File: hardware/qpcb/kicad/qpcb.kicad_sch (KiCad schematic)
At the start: 3 parts, among them J1 Conn_02x05_Odd_Even, J2 Conn_01x04, U1 Pico

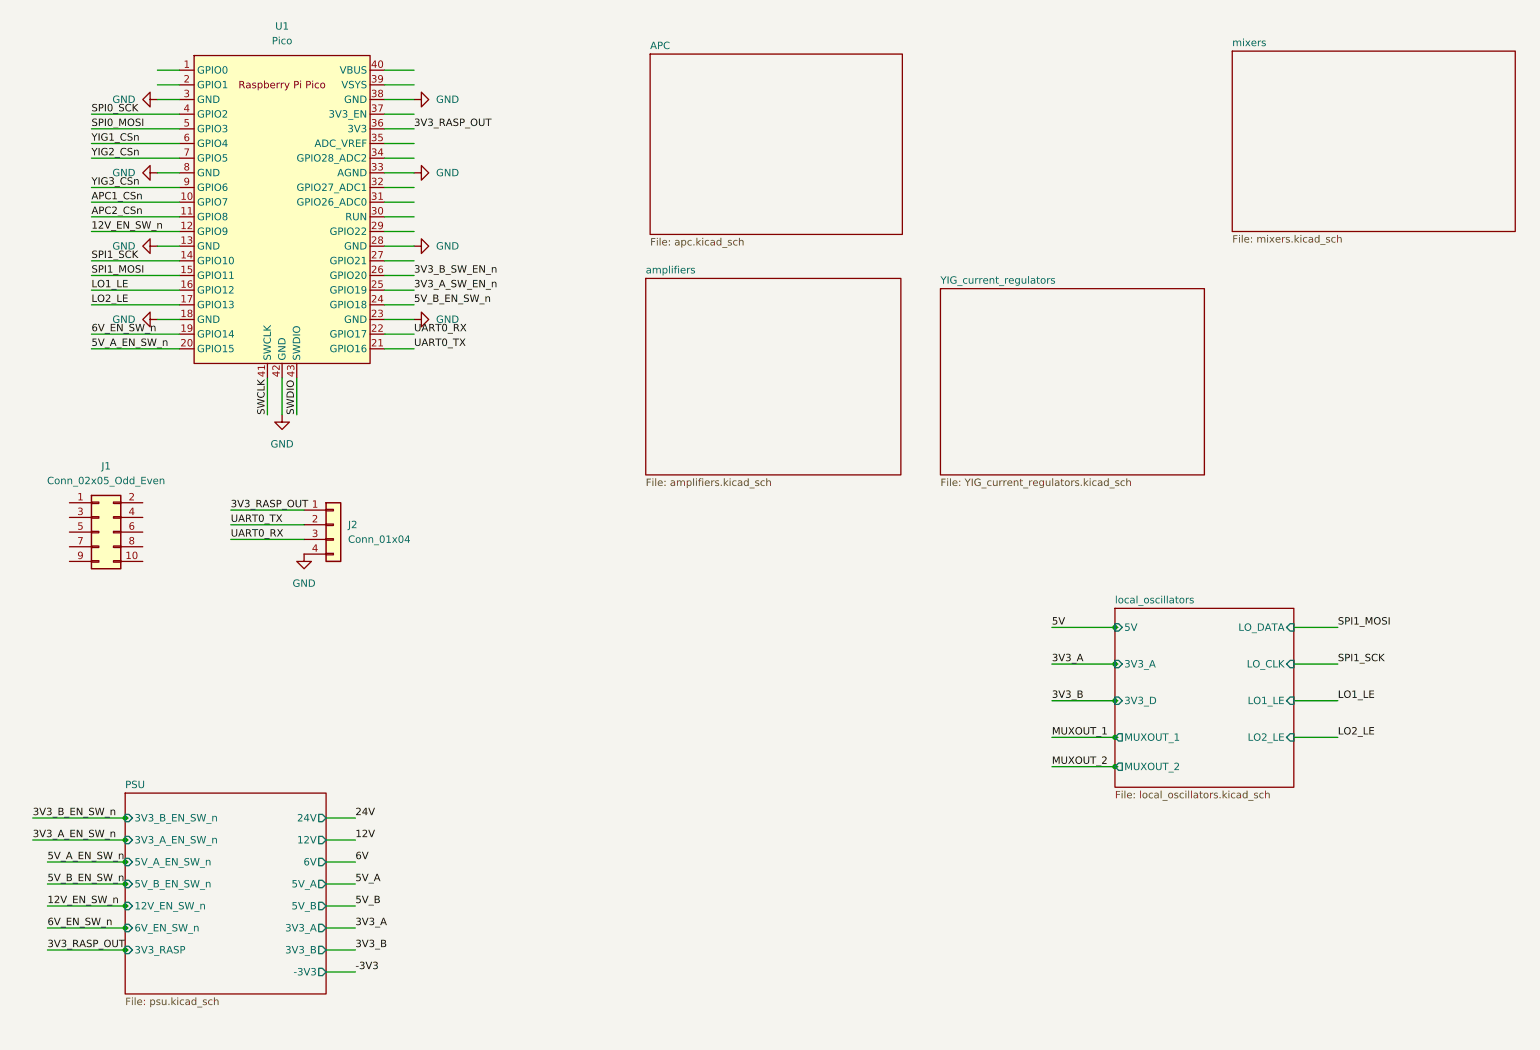
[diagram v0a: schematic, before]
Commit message: Complete PSU simulations and fix ERC errors
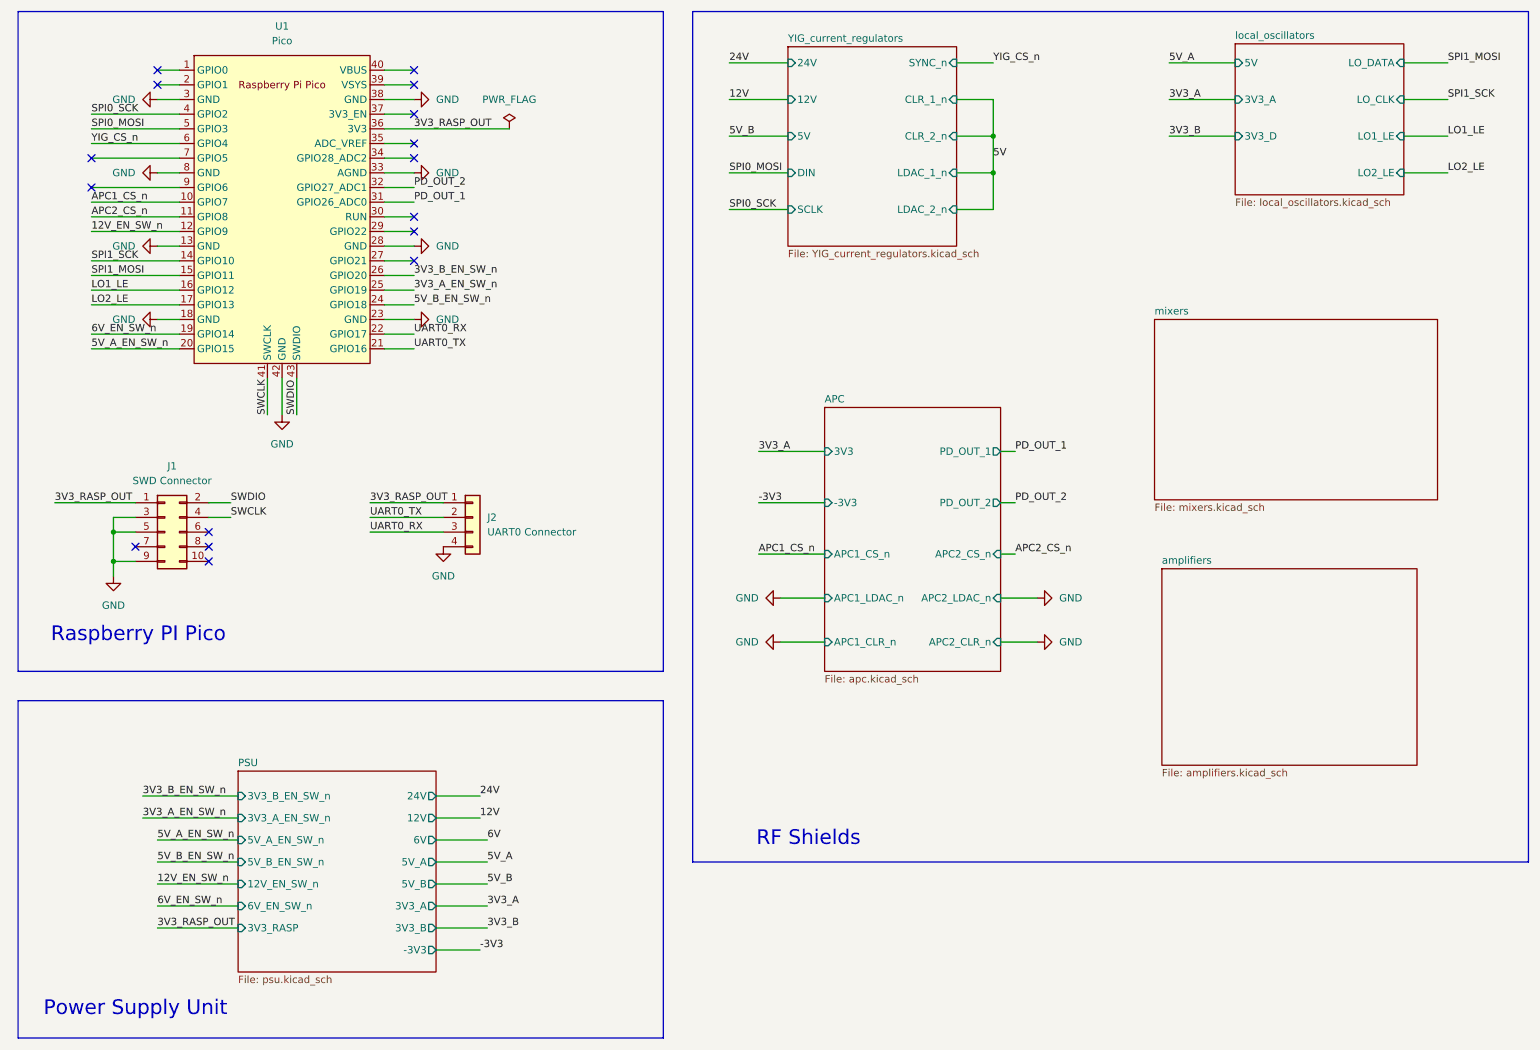
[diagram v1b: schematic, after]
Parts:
- J1: value Conn_02x05_Odd_Even -> SWD Connector
- J2: value Conn_01x04 -> UART0 Connector
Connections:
- net 3V3_A_SW_EN_n is gone; now on net 3V3_A_EN_SW_n: U1.25 (GPIO19)
- net 3V3_B_SW_EN_n is gone; now on net 3V3_B_EN_SW_n: U1.26 (GPIO20)
- net 3V3_RASP_OUT: now also J1.1 (Pin_1)
- net GND: now also J1.3 (Pin_3), J1.5 (Pin_5), J1.9 (Pin_9)
- net SWCLK: now also J1.4 (Pin_4)
- net SWDIO: now also J1.2 (Pin_2)
- net PD_OUT_1: now reaches U1.31 (GPIO26_ADC0)
- net PD_OUT_2: now reaches U1.32 (GPIO27_ADC1)
- net APC1_CSn renamed APC1_CS_n
- net APC2_CSn renamed APC2_CS_n
- net YIG1_CSn renamed YIG_CS_n
- net YIG2_CSn: no longer names the net of U1.7 (GPIO5)
- net YIG3_CSn: no longer names the net of U1.9 (GPIO6)
- no-connect marks 0 -> 16
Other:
- sheet APC ports: added -3V3, 3V3, APC1_CLR_n, APC1_CS_n, APC1_LDAC_n, APC2_CLR_n, APC2_CS_n, APC2_LDAC_n, PD_OUT_1, PD_OUT_2; removed none
- sheet YIG_current_regulators ports: added 12V, 24V, 5V, CLR_1_n, CLR_2_n, DIN, LDAC_1_n, LDAC_2_n, SCLK, SYNC_n; removed none
- sheet local_oscillators ports: added none; removed MUXOUT_1, MUXOUT_2
- note added: "Power Supply Unit"
- note added: "RF Shields"
- note added: "Raspberry PI Pico"
- moved on the sheet: J1, J2

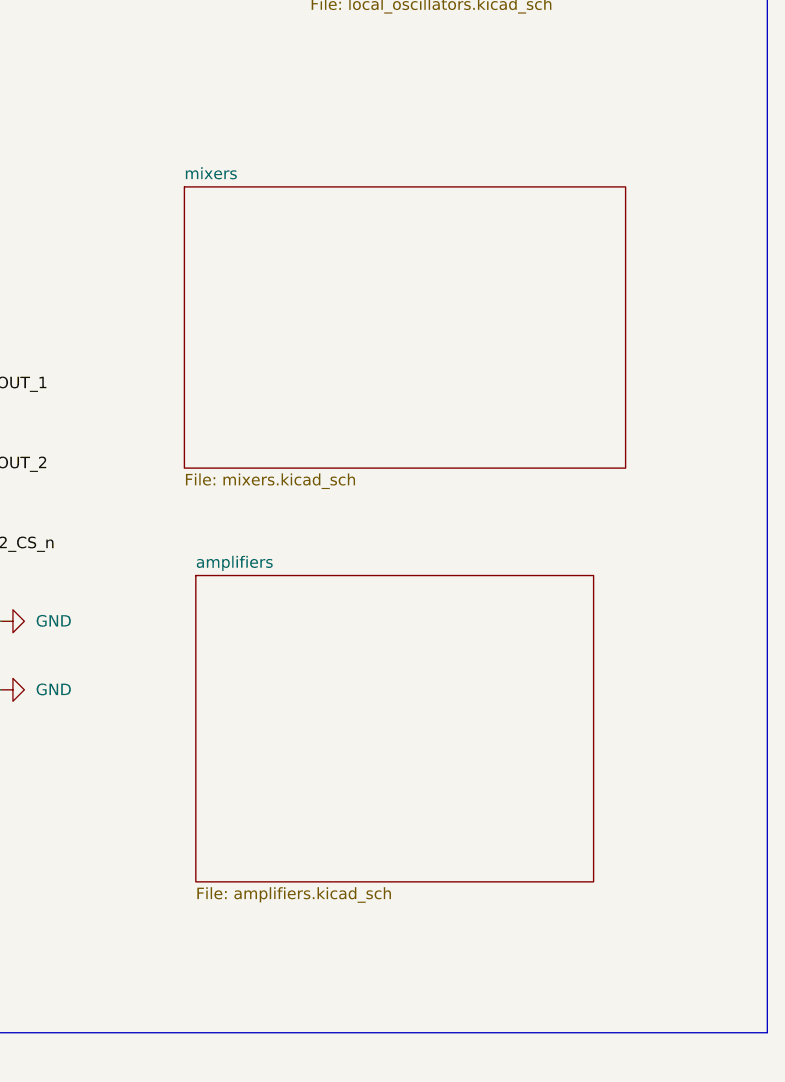
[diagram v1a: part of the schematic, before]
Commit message: Add mixer footprint and symbols
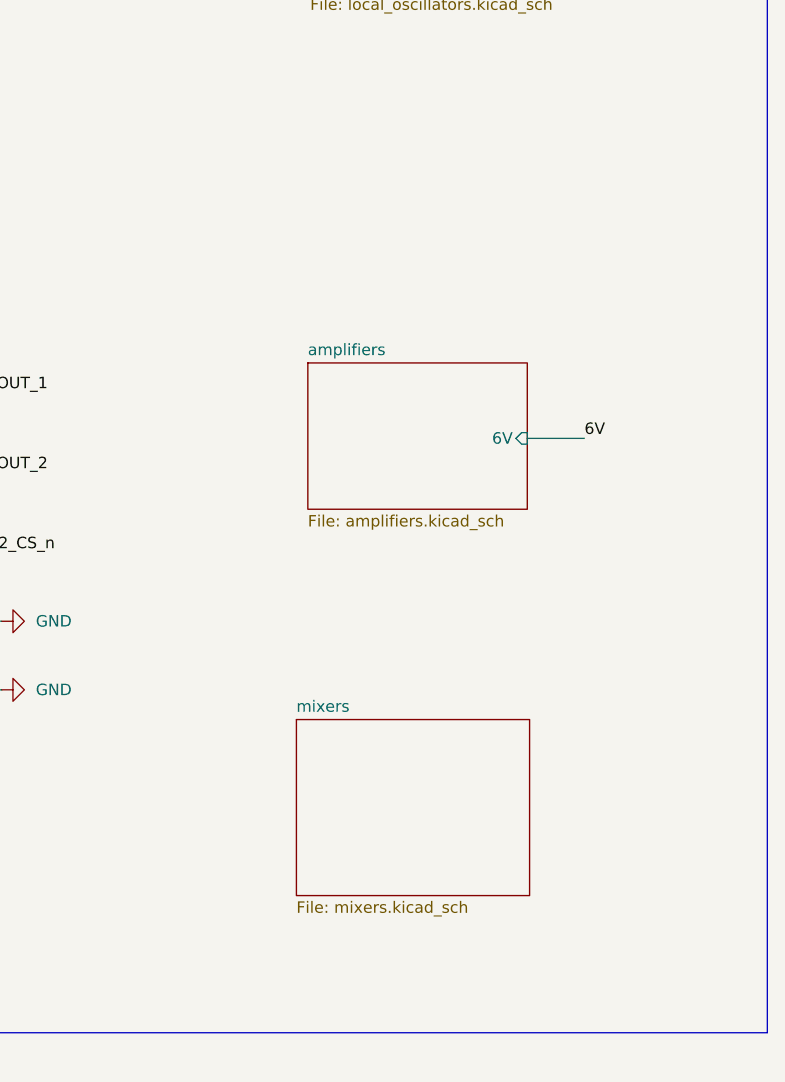
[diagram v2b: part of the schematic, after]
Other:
- sheet amplifiers ports: added 6V; removed none
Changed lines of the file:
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@@
+	(wire
+		(pts
+			(xy 252.73 96.52) (xy 259.08 96.52)
+		)
+		(stroke
+			(width 0)
+			(type default)
+		)
+	)
 	(wire
 		(pts
@@
 	(label "-3V3"
 		(at 146.05 100.33 0)
+		(fields_autoplaced yes)
+		(effects
+			(font
+				(size 1.27 1.27)
+			)
+			(justify left bottom)
+		)
+	)
+	(label "6V"
+		(at 259.08 96.52 0)
 		(fields_autoplaced yes)
 		(effects
@@
 	)
 	(sheet
-		(at 214.63 68.58)
-		(size 49.022 31.242)
+		(at 227.076 127.762)
+		(size 25.908 19.558)
 		(fields_autoplaced yes)
 		(stroke
@@
 		)
 		(property "Sheetname" "mixers"
-			(at 214.63 67.8684 0)
+			(at 227.076 127.0504 0)
 			(effects
 				(font
@@
 		)
 		(property "Sheetfile" "mixers.kicad_sch"
-			(at 214.63 100.4066 0)
+			(at 227.076 147.9046 0)
 			(effects
 				(font
@@
 	)
 	(sheet
-		(at 215.9 111.76)
-		(size 44.196 34.036)
+		(at 228.346 88.138)
+		(size 24.384 16.256)
 		(fields_autoplaced yes)
 		(stroke
@@
 		)
 		(property "Sheetname" "amplifiers"
-			(at 215.9 111.0484 0)
+			(at 228.346 87.4264 0)
 			(effects
 				(font
@@
 		)
 		(property "Sheetfile" "amplifiers.kicad_sch"
-			(at 215.9 146.3806 0)
+			(at 228.346 104.9786 0)
 			(effects
 				(font
@@
 			)
 		)
+		(pin "6V" input
+			(at 252.73 96.52 0)
+			(effects
+				(font
+					(size 1.27 1.27)
+				)
+				(justify right)
+			)
+		)

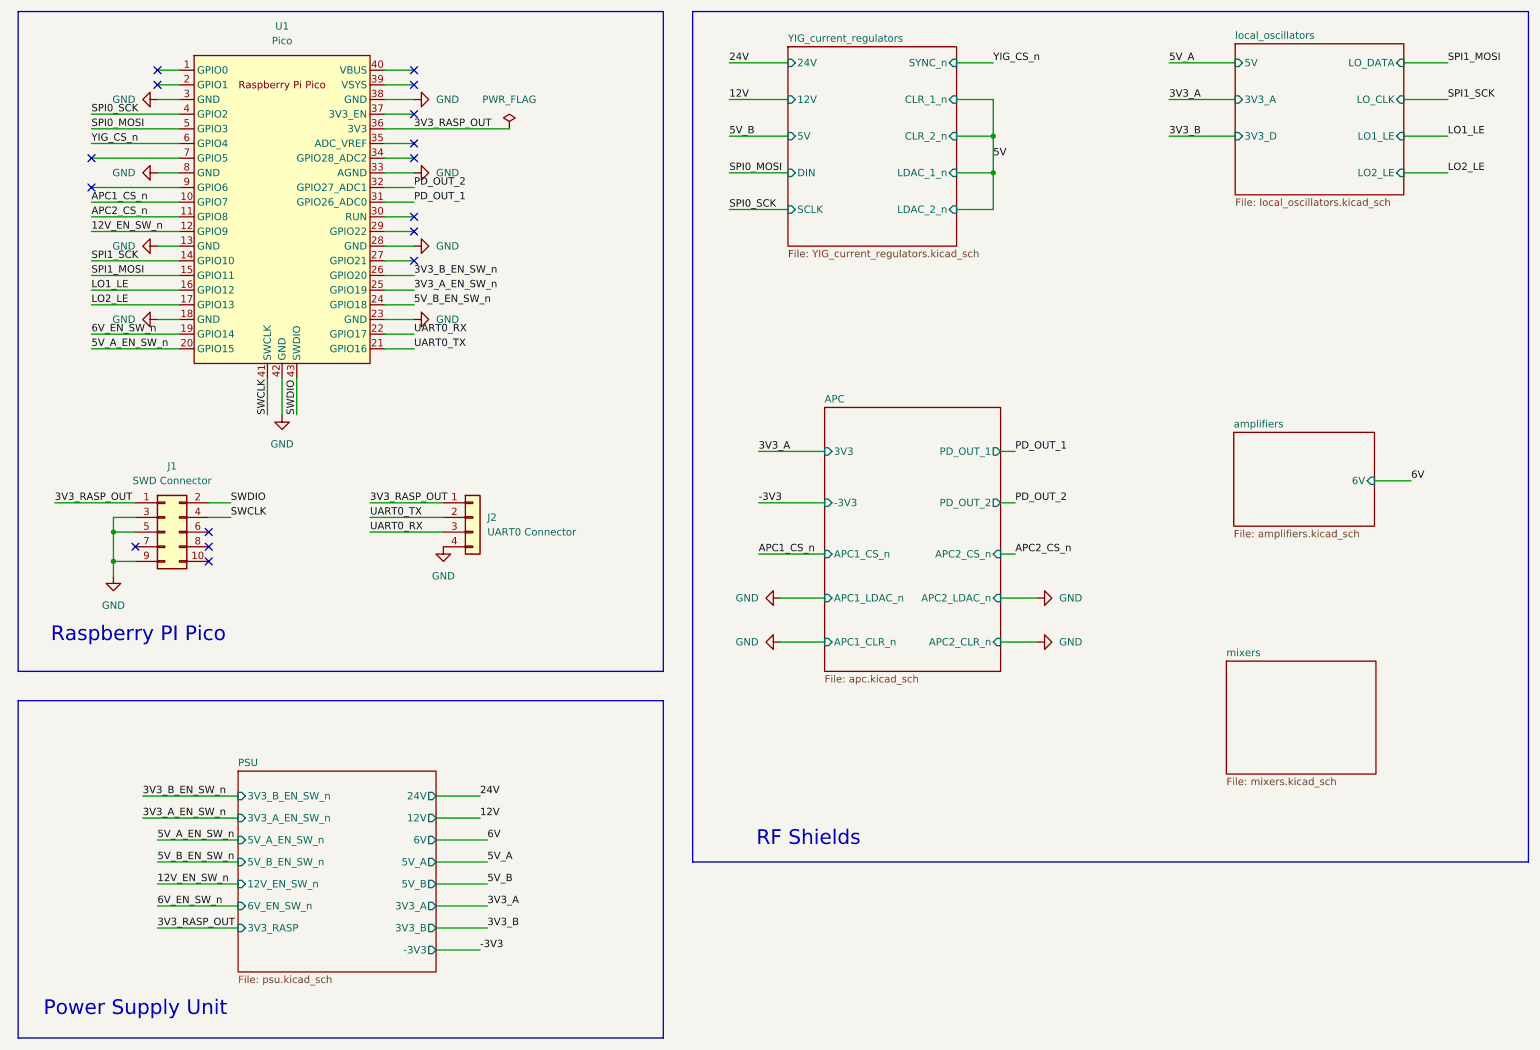
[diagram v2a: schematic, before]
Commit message: Final version of MC43063A and fill components' production info
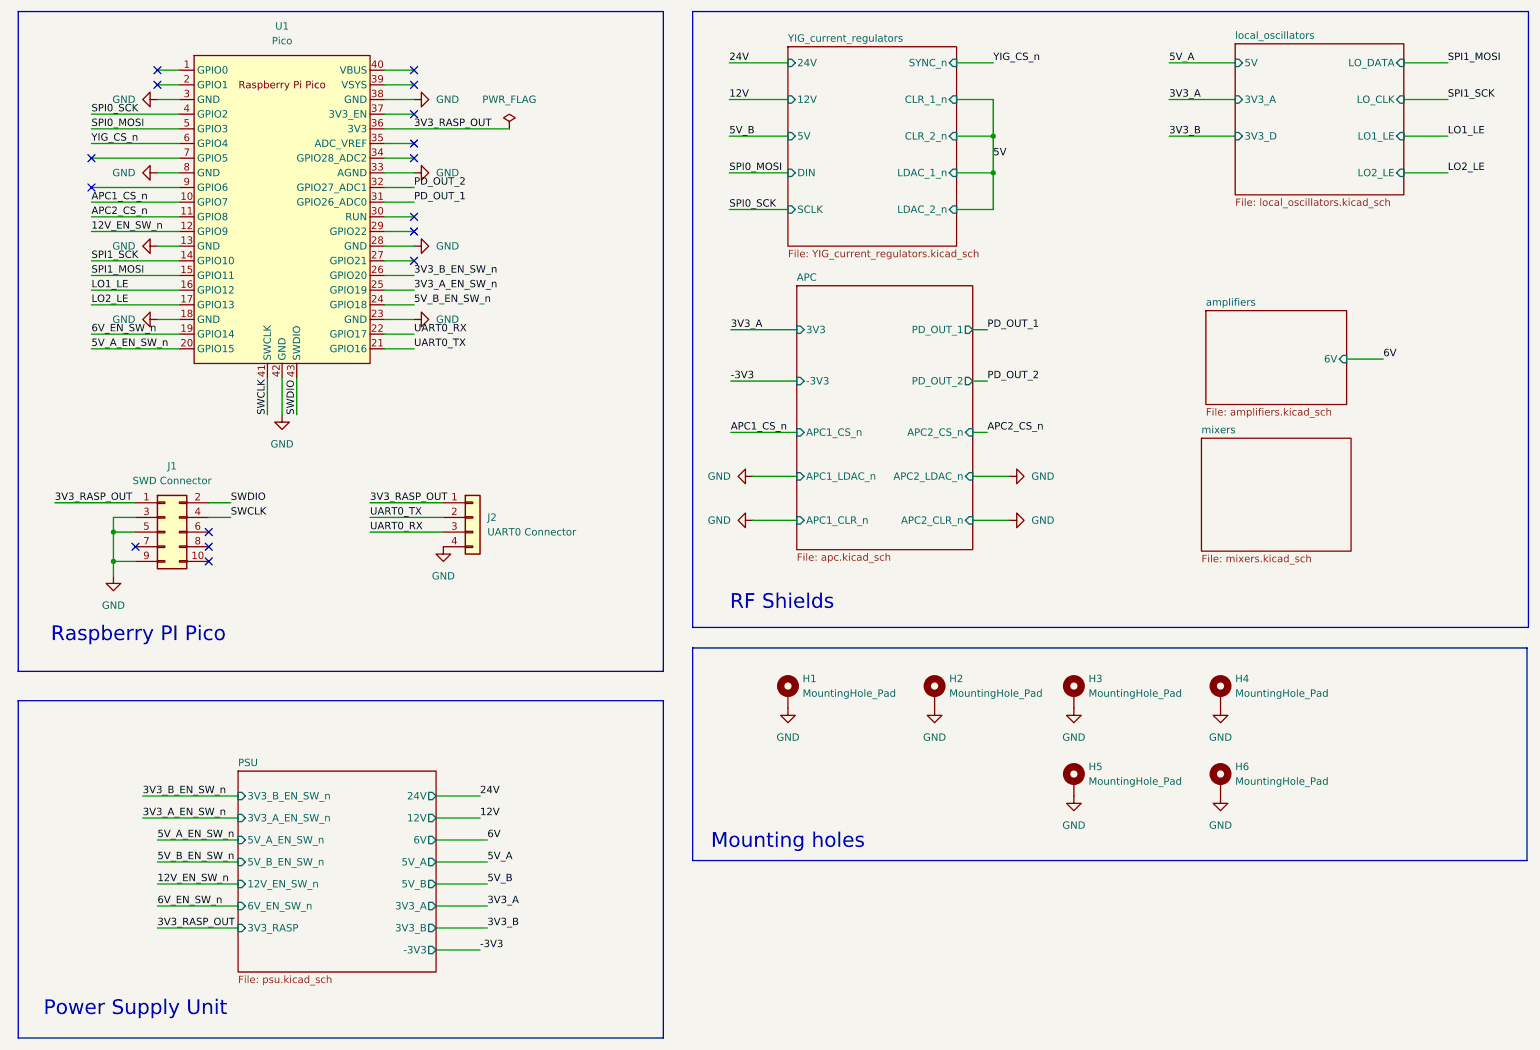
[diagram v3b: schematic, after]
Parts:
- added H1, H2, H3, H4, H5, H6: MountingHole_Pad, symbol Mechanical:MountingHole_Pad
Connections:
- net GND: now also H1.1, H2.1, H3.1, H4.1, H5.1, H6.1
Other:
- note added: "Mounting holes"
